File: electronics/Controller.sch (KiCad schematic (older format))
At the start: 12 parts, among them J1 Input 5v, U1 Pro Micro 32U4 USB

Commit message: Moving controller to Teensy++ 2.0
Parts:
- removed 1.8": TFT LCD ST7735S, symbol Connector_Generic_MountingPin:Conn_01x07_MountingPin
- removed U1: Pro Micro 32U4 USB, symbol ProMicro:ProMicro
- added IC1: Teensy++2.0, symbol teensy++20:Teensy++2.0
- added LCD: 8 pin, symbol Connector:Conn_01x08_Female
- added R? (x2): 1K, symbol Device:R
- Control, Password: GND (none) -> GND; Vcc (none) -> Vcc
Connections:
- wire segments 72 -> 73
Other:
- note removed: "GND\n\nVcc"
- note removed: "LED\nSCK\nSDA\nA0\nRESET\nCS\nGND\nVCC"
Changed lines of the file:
@@
 $EndDescr
-$Comp
-L ProMicro:ProMicro U1
-U 1 1 5E755F83
-P 3300 3100
-F 0 "U1" H 3300 4137 60  0001 C CNN
-F 1 "Pro Micro 32U4 USB" H 3300 4031 60  0000 C CNN
-F 2 "" H 3400 2050 60  0000 C CNN
-F 3 "" H 3400 2050 60  0000 C CNN
-F 4 "A0" H 3600 3150 50  0000 C CNN "A0"
-F 5 "A1" H 3600 3250 50  0000 C CNN "A1"
-F 6 "A2" H 3600 3350 50  0000 C CNN "A2"
-F 7 "A3" H 3600 3450 50  0000 C CNN "A3"
-F 8 "SCLK" H 3550 3050 50  0000 C CNN "SCLK"
-F 9 "MISO" H 3550 2950 50  0000 C CNN "MISO"
-F 10 "MOSI" H 3550 2850 50  0000 C CNN "MOSI"
-F 11 "A10" H 3550 2750 50  0000 C CNN "A10"
-F 12 "A6" H 3000 3250 50  0000 C CNN "A6"
-F 13 "A7" H 3000 3050 50  0000 C CNN "A7"
-F 14 "A8" H 3000 2850 50  0000 C CNN "A8"
-F 15 "A9" H 3000 2750 50  0000 C CNN "A9"
-	1    3300 3100
-	1    0    0    -1
-$EndComp
 $Comp
 L Device:R R?
@@
 L Connector_Generic:Conn_01x02 J1
 U 1 1 5E771D4E
-P 1400 2050
-F 0 "J1" H 1318 1725 50  0000 C CNN
-F 1 "Input 5v" H 1318 1816 50  0000 C CNN
-F 2 "" H 1400 2050 50  0001 C CNN
-F 3 "~" H 1400 2050 50  0001 C CNN
-F 4 "GND" H 1150 2000 50  0000 C CNN "2"
-F 5 "Vcc" H 1150 1900 50  0000 C CNN "1"
-	1    1400 2050
+P 1400 1650
+F 0 "J1" H 1318 1325 50  0001 C CNN
+F 1 "Input 5v" H 1318 1416 50  0000 C CNB
+F 2 "" H 1400 1650 50  0001 C CNN
+F 3 "~" H 1400 1650 50  0001 C CNN
+F 4 "GND" H 1150 1600 50  0000 C CNN "2"
+F 5 "Vcc" H 1150 1500 50  0000 C CNN "1"
+	1    1400 1650
 	-1   0    0    1
 $EndComp
 Wire Wire Line
-	4000 3150 4250 3150
-Wire Wire Line
-	4900 3250 5050 3250
-Wire Wire Line
-	4900 3350 5150 3350
-Wire Wire Line
-	4900 3450 5300 3450
-Wire Wire Line
-	2600 3350 2450 3350
-Wire Wire Line
-	2600 3450 2550 3450
-Wire Wire Line
-	2550 3450 2550 3650
-Wire Wire Line
-	4900 3550 5300 3550
-Wire Wire Line
-	4900 3650 5300 3650
-Wire Wire Line
-	2450 3350 2450 3550
+	3900 2750 4500 2750
+Wire Wire Line
+	4900 3250 4950 3250
+Wire Wire Line
+	4900 3350 5050 3350
+Wire Wire Line
+	4900 3450 5350 3450
+Wire Wire Line
+	4900 3550 5350 3550
 Wire Notes Line style solid rgb(132, 0, 0)
 	5550 2950 5550 4000
@@
 Wire Notes Line style solid rgb(132, 0, 0)
 	6900 2950 5550 2950
-Text Notes 5600 3750 0    51   ~ 0
-LED\nSCK\nSDA\nA0\nRESET\nCS\nGND\nVCC
-Wire Wire Line
-	4250 3150 4250 3250
-Wire Wire Line
-	5250 3750 5300 3750
-Wire Wire Line
-	4000 3350 4600 3350
-Wire Wire Line
-	4000 3450 4600 3450
-Wire Wire Line
-	2450 3550 4600 3550
-Wire Wire Line
-	2550 3650 4600 3650
-Wire Wire Line
-	4150 2350 4000 2350
-Wire Wire Line
-	4000 2650 5250 2650
-Wire Wire Line
-	5250 2650 5250 3750
+Wire Wire Line
+	4500 2750 4500 3250
+Wire Wire Line
+	4450 3350 4600 3350
+Wire Wire Line
+	4400 3450 4600 3450
+Wire Wire Line
+	4150 2150 3900 2150
 $Comp
 L Device:Rotary_Encoder_Switch Control
 U 1 1 5E7EB2C9
 P 1300 2850
-F 0 "Control" H 1300 2600 50  0000 C CNN
+F 0 "Control" H 1300 2600 50  0000 C CNB
 F 1 "Rotary_Encoder_Switch" H 1300 3126 50  0001 C CNN
 F 2 "" H 1150 3010 50  0001 C CNN
@@
 F 5 "DT" H 950 2800 50  0000 C CNN "DT"
 F 6 "SW" H 950 2900 50  0000 C CNN "SW"
+F 7 "GND" H 1700 2700 50  0000 C CNN "GND"
+F 8 "Vcc" H 1700 2900 50  0000 C CNN "Vcc"
 	1    1300 2850
 	-1   0    0    1
 $EndComp
 Wire Wire Line
-	1600 2750 2600 2750
-Wire Wire Line
-	1600 2850 2600 2850
-Wire Wire Line
-	1600 2950 2600 2950
+	1600 2750 2050 2750
+Wire Wire Line
+	1600 2850 2050 2850
+Wire Wire Line
+	1600 2950 2050 2950
 Wire Wire Line
 	1000 2750 800  2750
 Wire Wire Line
-	800  2500 1600 2500
-Wire Wire Line
-	1600 2500 1600 2650
+	800  2500 1950 2500
 Wire Wire Line
 	1000 2950 700  2950
 Wire Wire Line
-	700  2950 700  1600
-Wire Wire Line
-	700  1600 5250 1600
-Wire Wire Line
-	5250 1600 5250 2650
-Connection ~ 5250 2650
+	700  2950 700  2400
 Wire Wire Line
 	800  2500 800  2750
@@
 Text Notes 7050 6950 0    50   ~ 0
 AVR 32U4        Keyboard Controller\nLCD TFT Display\nRotary Encoders
-Text Notes 1000 2950 2    57   ~ 0
-GND\n\nVcc
 $Comp
 L Device:R R?
@@
 	0    1    1    0
 $EndComp
-$Comp
-L Connector_Generic_MountingPin:Conn_01x07_MountingPin 1.8"
-U 1 1 5E75A7AF
-P 5500 3450
-F 0 "1.8\"" H 6150 3450 50  0000 L CNN
-F 1 "TFT LCD ST7735S" H 5950 3300 50  0000 L CNN
-F 2 "" H 5500 3450 50  0001 C CNN
-F 3 "~" H 5500 3450 50  0001 C CNN
-	1    5500 3450
-	1    0    0    -1
-$EndComp
-Wire Wire Line
-	4250 3250 4600 3250
-Wire Wire Line
-	4900 3150 5300 3150
-Wire Wire Line
-	4000 2750 4350 2750
-Wire Wire Line
-	4350 2750 4350 3150
-Wire Wire Line
-	4350 3150 4600 3150
-Wire Wire Line
-	1600 2050 1600 2500
-Connection ~ 1600 2500
-Wire Wire Line
-	1600 2650 2600 2650
-Wire Wire Line
-	1600 1950 4150 1950
-Wire Wire Line
-	4150 1950 4150 2350
+Wire Wire Line
+	4500 3250 4600 3250
+Wire Wire Line
+	4900 3150 5350 3150
+Wire Wire Line
+	4550 2450 4550 3150
+Wire Wire Line
+	4550 3150 4600 3150
+Wire Wire Line
+	1950 1650 1950 2500
+Wire Wire Line
+	1600 1550 1850 1550
+Wire Wire Line
+	4150 1550 4150 2150
 $Comp
 L Device:Rotary_Encoder_Switch Password
 U 1 1 5EA37447
 P 1300 3350
-F 0 "Password" H 1300 3100 50  0000 C CNN
+F 0 "Password" H 1300 3100 50  0000 C CNB
 F 1 "Rotary_Encoder_Switch" H 1300 3626 50  0001 C CNN
 F 2 "" H 1150 3510 50  0001 C CNN
@@
 F 5 "DT" H 900 3300 50  0000 C CNN "DT"
 F 6 "SW" H 900 3400 50  0000 C CNN "SW"
+F 7 "GND" H 1700 3200 50  0000 C CNN "GND"
+F 8 "Vcc" H 1700 3400 50  0000 C CNN "Vcc"
 	1    1300 3350
 	-1   0    0    1
@@
 	800  3250 1000 3250
 Connection ~ 800  2750
-Wire Wire Line
-	1600 3250 1850 3250
-Wire Wire Line
-	1850 3250 1850 3050
-Wire Wire Line
-	1850 3050 2600 3050
-Wire Wire Line
-	1600 3350 1950 3350
-Wire Wire Line
-	1950 3350 1950 3150
-Wire Wire Line
-	1950 3150 2600 3150
-Wire Wire Line
-	1600 3450 2050 3450
-Wire Wire Line
-	2050 3450 2050 3250
-Wire Wire Line
-	2050 3250 2600 3250
 $Comp
 L Connector_Generic:Conn_01x04 J?
@@
 	-1   0    0    -1
 $EndComp
-Text Notes 6900 3550 2    51   ~ 0
+Text Notes 6700 3550 2    51   ~ 0
 SCK\nMISO\nMOSI\nCS
 Wire Wire Line
-	5150 3350 5150 4050
-Wire Wire Line
-	5150 4050 7300 4050
+	5050 3350 5050 4050
+Wire Wire Line
+	5050 4050 7300 4050
 Wire Wire Line
 	7300 4050 7300 3450
 Wire Wire Line
 	7300 3450 7150 3450
-Connection ~ 5150 3350
-Wire Wire Line
-	5150 3350 5300 3350
-Wire Wire Line
-	4000 3050 4150 3050
-Wire Wire Line
-	4150 3050 4150 4150
-Wire Wire Line
-	4150 4150 7200 4150
-Wire Wire Line
-	7200 4150 7200 3550
+Connection ~ 5050 3350
+Wire Wire Line
+	4250 4600 4600 4600
+Wire Wire Line
+	7200 4600 7200 3550
 Wire Wire Line
 	7200 3550 7150 3550
@@
 	7150 3350 7400 3350
 Wire Wire Line
-	7400 3350 7400 4250
-Wire Wire Line
-	7400 4250 4050 4250
-Wire Wire Line
-	4050 4250 4050 3250
-Wire Wire Line
-	4050 3250 4000 3250
+	7400 3350 7400 4700
+Wire Wire Line
+	7400 4700 4900 4700
 Wire Wire Line
 	7150 3250 7500 3250
@@
 	7500 3250 7500 4350
 Wire Wire Line
-	7500 4350 5050 4350
-Wire Wire Line
-	5050 4350 5050 3250
-Connection ~ 5050 3250
-Wire Wire Line
-	5050 3250 5300 3250
+	7500 4350 4950 4350
+Wire Wire Line
+	4950 4350 4950 3250
+Connection ~ 4950 3250
+Wire Wire Line
+	4950 3250 5350 3250
+$Comp
+L Device:R R?
+U 1 1 5EA68409
+P 4750 4600
+F 0 "R?" V 4543 4600 50  0001 C CNN
+F 1 "1K" V 4750 4600 50  0000 C CNN
+F 2 "" V 4680 4600 50  0001 C CNN
+F 3 "~" H 4750 4600 50  0001 C CNN
+	1    4750 4600
+	0    1    1    0
+$EndComp
+$Comp
+L Device:R R?
+U 1 1 5EA68789
+P 4750 4700
+F 0 "R?" V 4543 4700 50  0001 C CNN
+F 1 "1K" V 4750 4700 50  0000 C CNN
+F 2 "" V 4680 4700 50  0001 C CNN
+F 3 "~" H 4750 4700 50  0001 C CNN
+	1    4750 4700
+	0    1    1    0
+$EndComp
+Wire Wire Line
+	4900 4600 7200 4600
+Wire Wire Line
+	4250 4700 4600 4700
+$Comp
+L teensy++20:Teensy++2.0 IC1
+U 1 1 5EB23239
+P 3300 1900
+F 0 "IC1" H 3275 1915 50  0001 C CNN
+F 1 "Teensy++2.0" H 3275 1823 50  0000 C CNB
+F 2 "" H 3300 1900 50  0001 C CNN
+F 3 "" H 3300 1900 50  0001 C CNN
+	1    3300 1900
+	1    0    0    -1
+$EndComp
+Wire Wire Line
+	4350 3550 4600 3550
+Wire Wire Line
+	4300 3650 4600 3650
+Wire Wire Line
+	4450 3350 4450 2650
+Wire Wire Line
+	4450 2650 3900 2650
+$Comp
+L Connector:Conn_01x08_Female LCD
+U 1 1 5EB2D304
+P 5550 3450
+F 0 "LCD" H 6100 3450 50  0000 L CNB
+F 1 "8 pin" H 5578 3335 50  0001 L CNN
+F 2 "" H 5550 3450 50  0001 C CNN
+F 3 "~" H 5550 3450 50  0001 C CNN
+F 4 "Led" H 5650 3750 50  0000 C CNN "Led"
+F 5 "SCK" H 5650 3650 50  0000 C CNN "SCK"
+F 6 "SDA" H 5650 3550 50  0000 C CNN "SDA"
+F 7 "A0" H 5650 3450 50  0000 C CNN "A0"
+F 8 "Reset" H 5650 3350 50  0000 C CNN "Reset"
+F 9 "CS" H 5650 3250 50  0000 C CNN "CS"
+F 10 "GND" H 5650 3150 50  0000 C CNN "GND"
+F 11 "Vcc" H 5650 3050 50  0000 C CNN "Vcc"
+	1    5550 3450
+	1    0    0    -1
+$EndComp
+Wire Wire Line
+	4550 2450 3900 2450
+Wire Wire Line
+	5050 3350 5350 3350
+Wire Wire Line
+	4400 2350 3900 2350
+Wire Wire Line
+	4400 2350 4400 3450
+Wire Wire Line
+	4900 3650 5350 3650
+Wire Wire Line
+	3900 2850 4350 2850
+Wire Wire Line
+	4350 2850 4350 3550
+Wire Wire Line
+	4300 3650 4300 2950
+Wire Wire Line
+	4300 2950 3900 2950
+Wire Wire Line
+	1600 1650 1950 1650
+Connection ~ 1950 1650
+Wire Wire Line
+	1950 1650 2650 1650
+Wire Wire Line
+	1850 2400 1850 1550
+Wire Wire Line
+	700  2400 1850 2400
+Connection ~ 1850 1550
+Wire Wire Line
+	1850 1550 4150 1550
+Wire Wire Line
+	5350 3850 5150 3850
+Wire Wire Line
+	5150 3850 5150 1550
+Wire Wire Line
+	5150 1550 4150 1550
+Connection ~ 4150 1550
+Wire Wire Line
+	2650 1650 2650 2150
+Wire Wire Line
+	5350 3750 5250 3750
+Wire Wire Line
+	5250 3750 5250 1650
+Wire Wire Line
+	5250 1650 2650 1650
+Connection ~ 2650 1650
+Wire Wire Line
+	1600 3450 2050 3450
+Wire Wire Line
+	1600 3350 2050 3350
+Wire Wire Line
+	1600 3250 2050 3250
 $EndSCHEMATC

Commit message: Teensy++ 2.0 circuit rewrite
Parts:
- removed IC1: Teensy++2.0, symbol teensy++20:Teensy++2.0
- added IC1: Teensy++2.0, symbol teensy:Teensy++2.0-teensy++20
- LCD: A0 A0 -> A0 DC
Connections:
- wire segments 73 -> 78
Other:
- moved on the sheet: Control, LCD, Password

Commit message: circuit rewritten for Teensy++ 2.0
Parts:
- J?: symbol Connector_Generic:Conn_01x04 -> Connector:Conn_01x04_Female; CS (none) -> CS; MISO (none) -> MISO; MOSI (none) -> MOSI; SCK (none) -> SCK
- renumbered Password to Macro
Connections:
- net at R?.2: now also IC1.24 (PB4)
- net at R?.2: now also IC1.23 (PB3)
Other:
- note removed: "SCK\nMISO\nMOSI\nCS"
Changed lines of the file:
@@
 	6150 2100 6150 2700
 $Comp
-L Device:Rotary_Encoder_Switch Password
+L Device:Rotary_Encoder_Switch Macro
 U 1 1 5EA37447
 P 3300 3500
-F 0 "Password" H 3300 3250 50  0000 C CNB
+F 0 "Macro" H 3300 3250 50  0000 C CNB
 F 1 "Rotary_Encoder_Switch" H 3300 3776 50  0001 C CNN
 F 2 "" H 3150 3660 50  0001 C CNN
@@
 	2800 3400 3000 3400
 $Comp
-L Connector_Generic:Conn_01x04 J?
+L Connector:Conn_01x04_Female J?
 U 1 1 5EA4FC54
-P 8950 3900
-F 0 "J?" H 8868 3475 50  0001 C CNN
-F 1 "Conn_01x04" H 8868 3566 50  0001 C CNN
-F 2 "" H 8950 3900 50  0001 C CNN
-F 3 "~" H 8950 3900 50  0001 C CNN
-	1    8950 3900
+P 8900 4000
+F 0 "J?" H 8818 3575 50  0001 C CNN
+F 1 "Conn_01x04" H 8818 3666 50  0001 C CNN
+F 2 "" H 8900 4000 50  0001 C CNN
+F 3 "~" H 8900 4000 50  0001 C CNN
+F 4 "SCK" H 9050 4100 50  0000 C CNN "SCK"
+F 5 "MISO" H 9050 4000 50  0000 C CNN "MISO"
+F 6 "MOSI" H 9050 3900 50  0000 C CNN "MOSI"
+F 7 "CS" H 9050 3800 50  0000 C CNN "CS"
+	1    8900 4000
 	-1   0    0    -1
 $EndComp
-Text Notes 8700 4100 2    51   ~ 0
-SCK\nMISO\nMOSI\nCS
-Wire Wire Line
-	7050 3900 7050 4650
-Wire Wire Line
-	7050 4650 9300 4650
-Wire Wire Line
-	9300 4650 9300 4000
-Wire Wire Line
-	9300 4000 9150 4000
 Connection ~ 7050 3900
-Wire Wire Line
-	6250 5150 6600 5150
-Wire Wire Line
-	9200 5150 9200 4100
-Wire Wire Line
-	9200 4100 9150 4100
-Wire Wire Line
-	9150 3900 9400 3900
-Wire Wire Line
-	9400 3900 9400 5250
-Wire Wire Line
-	9400 5250 6900 5250
-Wire Wire Line
-	9150 3800 9500 3800
-Wire Wire Line
-	9500 3800 9500 4750
-Wire Wire Line
-	9500 4750 6950 4750
-Wire Wire Line
-	6950 4750 6950 3800
 Connection ~ 6950 3800
 Wire Wire Line
@@
 L Device:R R?
 U 1 1 5EA68409
-P 6750 5150
-F 0 "R?" V 6543 5150 50  0001 C CNN
-F 1 "1K" V 6750 5150 50  0000 C CNN
-F 2 "" V 6680 5150 50  0001 C CNN
-F 3 "~" H 6750 5150 50  0001 C CNN
-	1    6750 5150
+P 6750 3000
+F 0 "R?" V 6543 3000 50  0001 C CNN
+F 1 "1K" V 6750 3000 50  0000 C CNN
+F 2 "" V 6680 3000 50  0001 C CNN
+F 3 "~" H 6750 3000 50  0001 C CNN
+	1    6750 3000
 	0    1    1    0
 $EndComp
@@
 L Device:R R?
 U 1 1 5EA68789
-P 6750 5250
-F 0 "R?" V 6543 5250 50  0001 C CNN
-F 1 "1K" V 6750 5250 50  0000 C CNN
-F 2 "" V 6680 5250 50  0001 C CNN
-F 3 "~" H 6750 5250 50  0001 C CNN
-	1    6750 5250
+P 6750 3100
+F 0 "R?" V 6543 3100 50  0001 C CNN
+F 1 "1K" V 6750 3100 50  0000 C CNN
+F 2 "" V 6680 3100 50  0001 C CNN
+F 3 "~" H 6750 3100 50  0001 C CNN
+	1    6750 3100
 	0    1    1    0
 $EndComp
 Wire Wire Line
-	6900 5150 9200 5150
-Wire Wire Line
-	6250 5250 6600 5250
+	6900 3000 9500 3000
 Wire Wire Line
 	6500 4100 6600 4100
@@
 Wire Wire Line
 	4650 2200 7250 2200
+Wire Wire Line
+	6950 3200 6950 3800
+Wire Wire Line
+	5900 3100 6600 3100
+Wire Wire Line
+	6900 3100 9400 3100
+Wire Wire Line
+	9400 3100 9400 4000
+Wire Wire Line
+	9400 4000 9100 4000
+Wire Wire Line
+	9100 3900 9300 3900
+Wire Wire Line
+	9300 3900 9300 3200
+Wire Wire Line
+	6950 3200 9300 3200
+Wire Wire Line
+	9100 4100 9200 4100
+Wire Wire Line
+	9200 4100 9200 3300
+Wire Wire Line
+	9200 3300 7050 3300
+Wire Wire Line
+	7050 3300 7050 3900
+Wire Wire Line
+	6600 3000 5900 3000
+Wire Wire Line
+	9500 3000 9500 4200
+Wire Wire Line
+	9500 4200 9100 4200
 $EndSCHEMATC

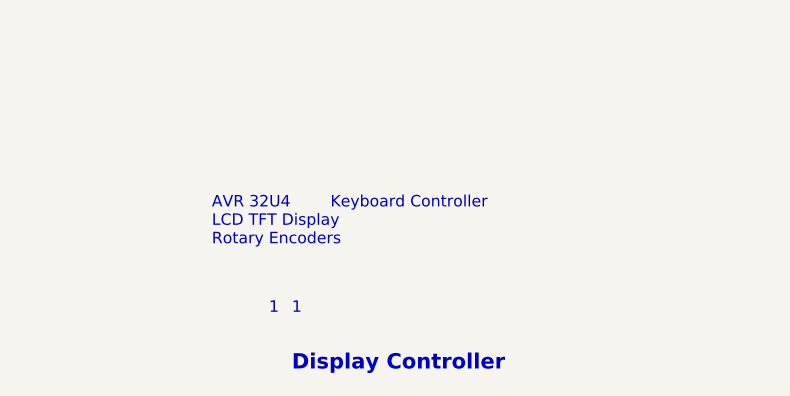
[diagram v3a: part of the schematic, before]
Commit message: Schematics description added
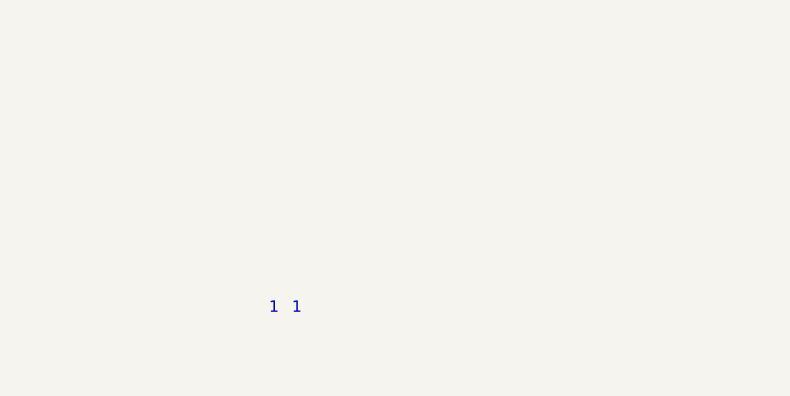
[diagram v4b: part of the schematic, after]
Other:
- note removed: "AVR 32U4 Keyboard Controller\nLCD TFT Display\nRotary Encoders"
- note removed: "Display Controller"
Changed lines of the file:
@@
 encoding utf-8
 Sheet 1 1
-Title ""
-Date ""
-Rev ""
+Title "Keyboard Controller"
+Date "2020"
+Rev "1.1"
 Comp "Ben"
-Comment1 ""
-Comment2 ""
-Comment3 ""
+Comment1 "Teensy++ 2.0"
+Comment2 "LCD TFT Display (with SD Card reader)"
+Comment3 "2 Rotary Encoders"
 Comment4 ""
 $EndDescr
@@
 Wire Wire Line
 	2800 3050 3950 3050
-Text Notes 7400 7500 0    67   ~ 13
-Display Controller
 Text Notes 7300 7250 0    50   ~ 0
 1
 Text Notes 7400 7250 0    50   ~ 0
 1
-Text Notes 7050 6950 0    50   ~ 0
-AVR 32U4        Keyboard Controller\nLCD TFT Display\nRotary Encoders
 $Comp
 L Device:R R?

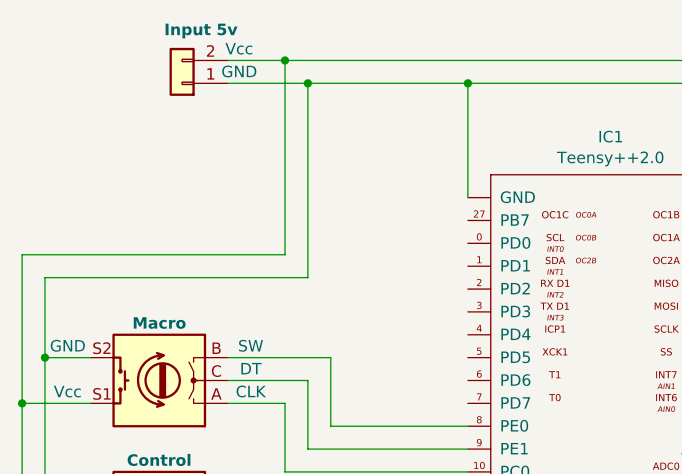
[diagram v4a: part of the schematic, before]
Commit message: Added serial port communication
Both ICs might exchange data through Serial1 port
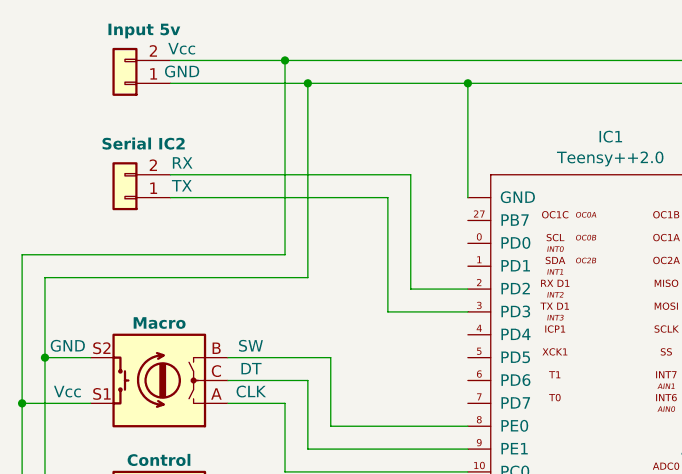
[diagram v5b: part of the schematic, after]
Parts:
- added J?: Serial IC2, symbol Connector_Generic:Conn_01x02
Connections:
- net at IC1.2 (PD2): now also J?.2 (Pin_2)
- net at IC1.3 (PD3): now also J?.1 (Pin_1)
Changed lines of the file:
@@
 L Connector_Generic:Conn_01x02 J1
 U 1 1 5E771D4E
-P 3400 2200
-F 0 "J1" H 3318 1875 50  0001 C CNN
-F 1 "Input 5v" H 3318 1966 50  0000 C CNB
-F 2 "" H 3400 2200 50  0001 C CNN
-F 3 "~" H 3400 2200 50  0001 C CNN
-F 4 "GND" H 3150 2150 50  0000 C CNN "2"
-F 5 "Vcc" H 3150 2050 50  0000 C CNN "1"
-	1    3400 2200
+P 3150 2200
+F 0 "J1" H 3068 1875 50  0001 C CNN
+F 1 "Input 5v" H 3068 1966 50  0000 C CNB
+F 2 "" H 3150 2200 50  0001 C CNN
+F 3 "~" H 3150 2200 50  0001 C CNN
+F 4 "GND" H 2900 2150 50  0000 C CNN "2"
+F 5 "Vcc" H 2900 2050 50  0000 C CNN "1"
+	1    3150 2200
 	-1   0    0    1
 $EndComp
@@
 	3950 2200 3950 3050
 Wire Wire Line
-	3600 2100 3850 2100
+	3350 2100 3850 2100
 Wire Wire Line
 	6150 2100 6150 2700
@@
 	6600 4200 6600 4600
 Wire Wire Line
-	3600 2200 3950 2200
+	3350 2200 3950 2200
 Connection ~ 3950 2200
 Wire Wire Line
@@
 Wire Wire Line
 	9500 4200 9100 4200
+$Comp
+L Connector_Generic:Conn_01x02 J?
+U 1 1 5F0993D1
+P 3150 2700
+F 0 "J?" H 3068 2375 50  0001 C CNN
+F 1 "Serial IC2" H 3068 2466 50  0000 C CNB
+F 2 "" H 3150 2700 50  0001 C CNN
+F 3 "~" H 3150 2700 50  0001 C CNN
+F 4 "TX" H 2900 2650 50  0000 C CNN "2"
+F 5 "RX" H 2900 2550 50  0000 C CNN "1"
+	1    3150 2700
+	-1   0    0    1
+$EndComp
+Wire Wire Line
+	3350 2600 4400 2600
+Wire Wire Line
+	4400 2600 4400 3100
+Wire Wire Line
+	4400 3100 4650 3100
+Wire Wire Line
+	3350 2700 4300 2700
+Wire Wire Line
+	4300 2700 4300 3200
+Wire Wire Line
+	4300 3200 4650 3200
 $EndSCHEMATC
